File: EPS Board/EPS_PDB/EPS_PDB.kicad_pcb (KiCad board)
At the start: 2 copper layers, 92 x 92 mm, 125 parts, among them J1 USB_B_Micro, J2 Conn_02x26_Odd_Even, J3 Conn_02x26_Odd_Even, J4 Conn_01x04_Pin, Q1 PMOS, Q2 PMOS, SW1 SW_SPDT, U1 AMS1117-3.3, U10 TPS259621DDAT, U11 LM5000-3MTCX, U12 TPS259621DDAT, U13 TPS259621DDAT, U14 AD7708BRUZ, U15 TPS259621DDAT, U16 TPS259621DDAT, U17 LTC3624EMSE-3.3PBF, U18 TPS259621DDAT, U19 LTC3624IDD-25PBF, U2 SN65HVD256D, U3 SN65HVD256D, U4 STM32L476VET6, U5 TPS3824-33QDBVRQ1, U6 TS4061BICT-1.25, U7 TPS259621DDAT, U8 TPS259621DDAT, U9 TPS259621DDAT, Y1 32MHz, Y2 32.768kHz

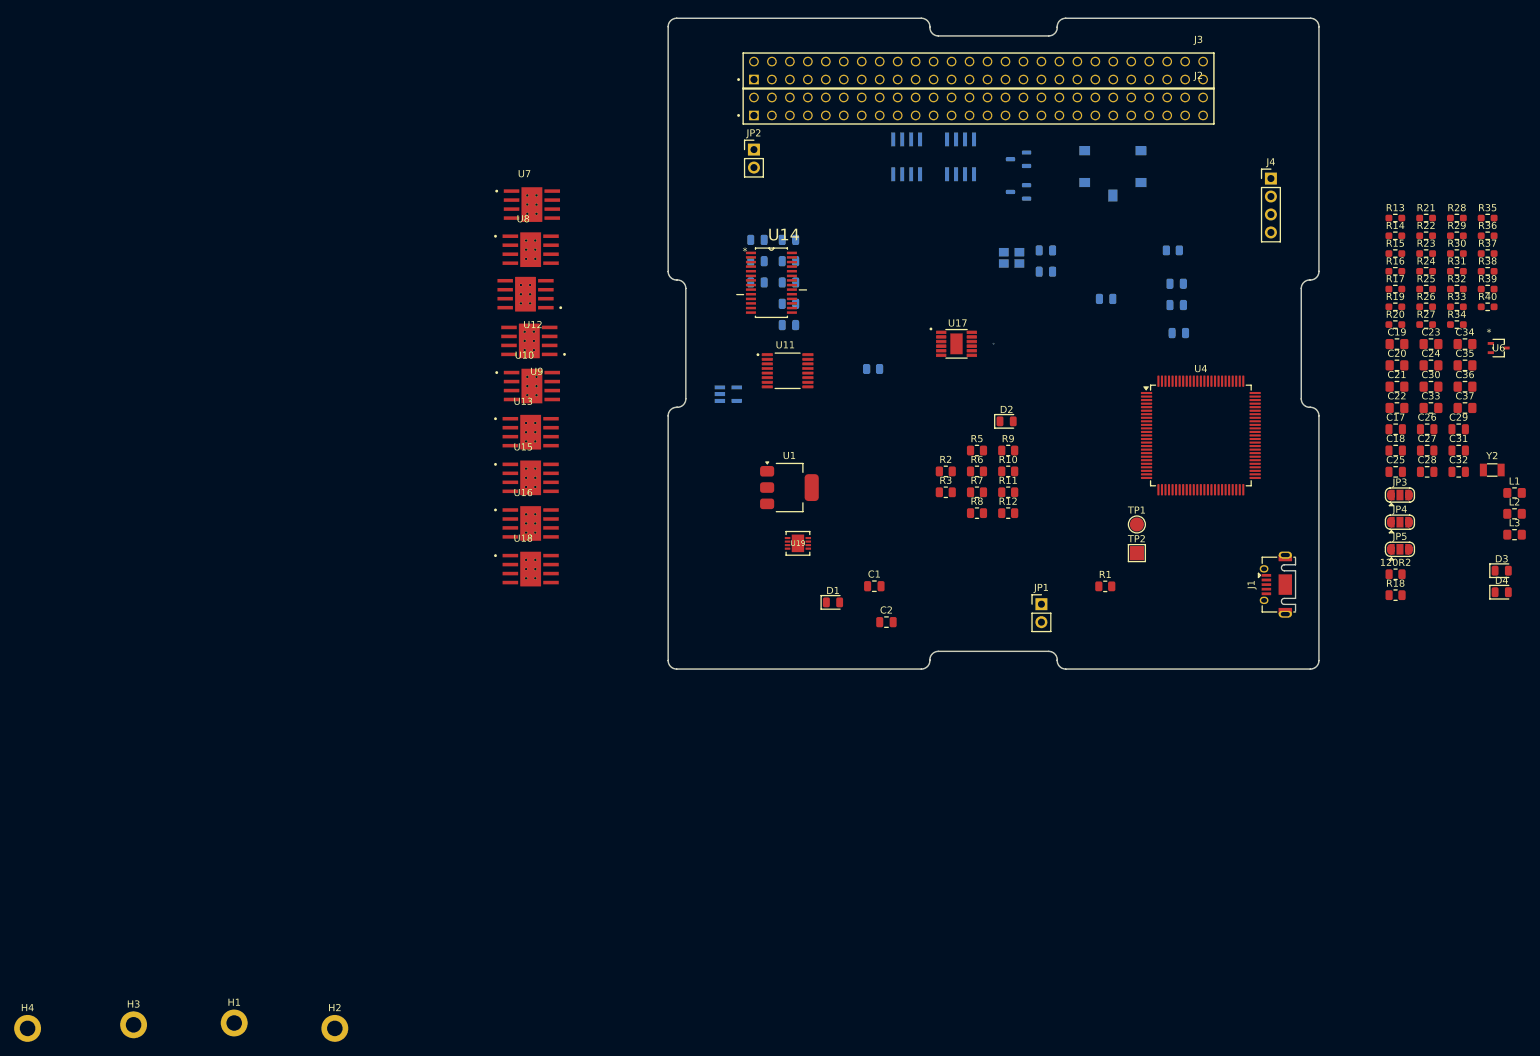
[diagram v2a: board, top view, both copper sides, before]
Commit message: PDB PCB Design Progress
Board outline copy pasted from Antenna Deployment Board
Added current limiter datasheet
Routed USB differential pair
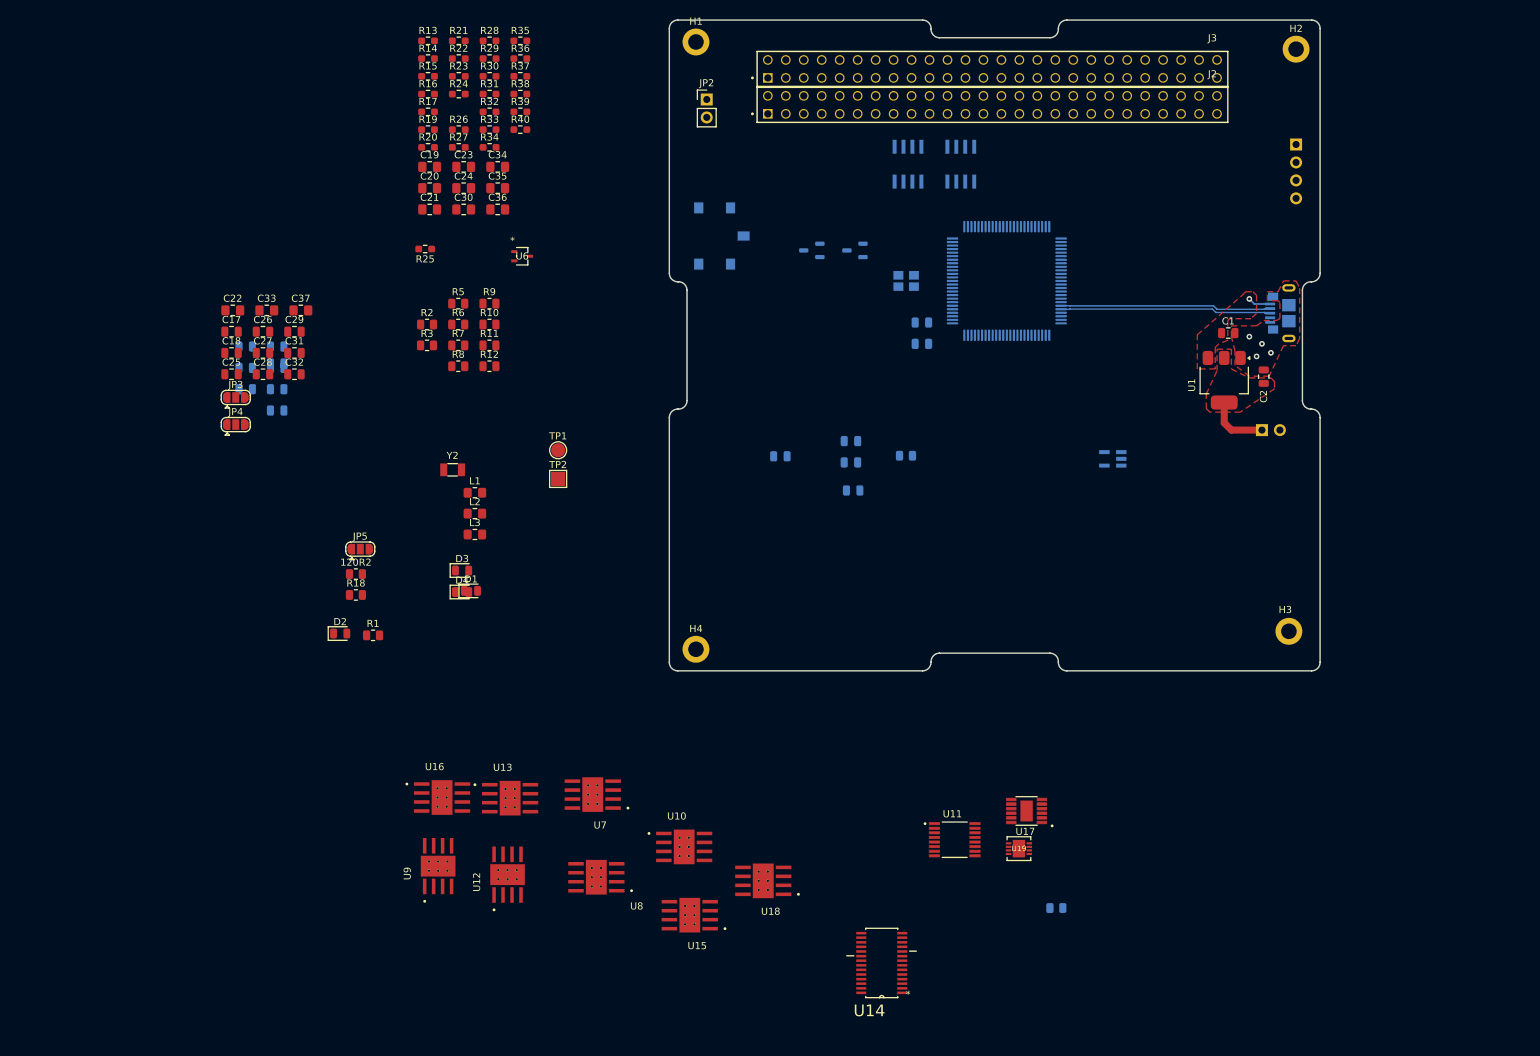
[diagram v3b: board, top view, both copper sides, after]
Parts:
- J1: footprint Connector_USB:USB_Micro-AB_Molex_47590-0001 -> Connector_USB:USB_Micro-B_GCT_USB3076-30-A; moved to B.Cu
- J4, JP1, U4: moved to B.Cu
- U10: value TPS259621DDAT -> TPS259621DDAT_5V_PAY
- U12: value TPS259621DDAT -> TPS259621DDAT_5V_EPS
- U13: value TPS259621DDAT -> TPS259621DDAT_5V_OBC
- U15: value TPS259621DDAT -> TPS259621DDAT_5V_ADCS
- U16: value TPS259621DDAT -> TPS259621DDAT_5V_COMM
- U18: value TPS259621DDAT -> TPS259621DDAT_12V_ADCS
- U7: value TPS259621DDAT -> TPS259621DDAT 3V3_ADCS
- U8: value TPS259621DDAT -> TPS259621DDAT_3V3_ANT
- U9: value TPS259621DDAT -> TPS259621DDAT_3V3_EPS
- moved H2 194.0 mm to (202.2, 49.8)
- moved H3 172.5 mm to (201.2, 132.1)
- moved C22 165.2 mm to (51.9, 86.7)
- moved C29 165.2 mm to (60.6, 89.7)
- moved C31 165.2 mm to (60.6, 92.7)
- moved C32 165.2 mm to (60.6, 95.7)
- moved C33 165.2 mm to (56.7, 86.7)
- moved C17 165.2 mm to (51.7, 89.7)
- moved C18 165.2 mm to (51.7, 92.7)
- moved C25 165.2 mm to (51.7, 95.7)
- moved C26 165.2 mm to (56.1, 89.7)
- moved C27 165.2 mm to (56.1, 92.7)
- moved C28 165.2 mm to (56.1, 95.7)
- moved C37 165.2 mm to (61.5, 86.7)
- moved JP3 165.2 mm to (52.3, 99.0)
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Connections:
- net Net-(U11-FB) renamed /EPS Power Distribution/12V
- net Net-(U11-VIN) renamed /EPS Power Distribution/VIN
- J1 pad 6: unconnected-(J1-Shield-Pad6) -> GND
- U4 pad 70: /EPS Control Unit/USB_D- -> /USB_D-
- U4 pad 71: /EPS Control Unit/USB_D+ -> /USB_D+
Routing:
- net /USB_D-: track 0.00 -> 30.1 mm
- net /USB_D+: track 0.00 -> 30.1 mm
- net /3V3_LDO: track 0.00 -> 8.63 mm
- net VBUS: track 0.00 -> 3.57 mm, vias 0 -> 1
- net GND: vias 0 -> 4
- added copper zone on F.Cu, net /3V3_LDO
- added copper zone on F.Cu, net GND
- added copper zone on In1.Cu, net GND
- added copper zone on F.Cu, net VBUS
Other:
- outline, holes or cut-outs redrawn
- copper layers 2 -> 4
- board text added: "4 LAYER BOARD SIG+PWR GND GND SIG"

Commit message: EPS PDB Board Layout Progress
Fixed issue with outline,
added correct outline
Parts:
- added D5: EPS_5V_LED, LED_SMD:LED_0805_2012Metric, B.Cu at (167.7, 102.4)
- added JP6: USB_POW_EN, Connector_PinHeader_2.54mm:PinHeader_1x02_P2.54mm_Vertical, F.Cu at (187.8, 82.4)
- added R41: 1k5, Resistor_SMD:R_0603_1608Metric, B.Cu at (163.5, 102.4)
- C1, C2: footprint Capacitor_SMD:C_0805_2012Metric -> Capacitor_SMD:C_0603_1608Metric; moved to B.Cu
- C10, C11, C12, C13, C14, C15, C16, C17, C18, C25, C26, C27, C28, C29, C3, C31, C32, C4, C5, C6, C7, C8, C9: footprint Capacitor_SMD:C_0805_2012Metric -> Capacitor_SMD:C_0603_1608Metric
- C19, C20, C21, C22, C23, C24, C30, C33, C34, C35, C36, C37: footprint Capacitor_SMD:C_0805_2012Metric_Pad1.18x1.45mm_HandSolder -> Capacitor_SMD:C_0603_1608Metric
- D1: value POWER_LED -> EPS_3V3_LED; moved to B.Cu
- D2, U1: moved to B.Cu
- H1, H2, H3, H4: footprint MountingHole:MountingHole_2.2mm_M2_DIN965_Pad -> MountingHole:MountingHole_3.2mm_M3_Pad
- J4: footprint Connector_PinHeader_2.54mm:PinHeader_1x04_P2.54mm_Vertical -> Connector_PinHeader_2.54mm:PinHeader_1x04_P2.54mm_Horizontal; moved to F.Cu
- JP1: moved to F.Cu
- R1, R11, R12, R7, R8: footprint Resistor_SMD:R_0805_2012Metric -> Resistor_SMD:R_0603_1608Metric; moved to B.Cu
- R10, R18, R2, R3, R4, R5, R6, R9: footprint Resistor_SMD:R_0805_2012Metric -> Resistor_SMD:R_0603_1608Metric
- R13, R14, R15, R16, R17, R19, R20, R21, R22, R23, R24, R25, R26, R27, R28, R29, R30, R31, R32, R33, R34, R35, R36, R37, R38, R39, R40: footprint Resistor_SMD:R_0603_1608Metric_Pad0.98x0.95mm_HandSolder -> Resistor_SMD:R_0603_1608Metric
- moved U10 219.2 mm to (-102.7, 143.9)
- moved U11 219.2 mm to (-64.4, 142.9)
- moved U12 219.2 mm to (-127.7, 147.8)
- moved U13 219.2 mm to (-127.3, 137.0)
- moved U14 219.2 mm to (-74.7, 160.3)
- moved U15 219.2 mm to (-101.9, 153.6)
- moved U16 219.2 mm to (-136.9, 136.9)
- moved U17 219.2 mm to (-54.3, 138.8)
- moved U18 219.2 mm to (-91.5, 148.7)
- moved U19 219.2 mm to (-55.4, 144.1)
- moved U7 219.2 mm to (-115.6, 136.5)
- moved U8 219.2 mm to (-115.1, 148.2)
- moved U9 219.2 mm to (-137.5, 146.6)
- moved TP1 176.3 mm to (-78.3, 112.2)
- moved TP2 176.3 mm to (-78.3, 116.2)
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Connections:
- C1 pad 1: VBUS -> VUSB
- C34 pad 1: VBUS -> /VBUS
- C36 pad 1: VBUS -> /VBUS
- J1 pad 1: VBUS -> VUSB
- J1 pad 6: GND -> unconnected-(J1-Shield-Pad6)_5
- J3 pad 52: /I2C2_SDA -> /I2C1_SDA
- JP2 pad 2: VBUS -> /VBUS
- JP3 pad 2: Net-(JP3-C) -> Net-(JP3-B)
- JP5 pad 2: Net-(JP5-C) -> Net-(JP5-B)
- L1 pad 1: VBUS -> /VBUS
- R25 pad 2: VBUS -> /VBUS
- R8 pad 2: /I2C2_SDA -> /I2C1_SDA
- U1 pad 3: VBUS -> VUSB
- U17 pad 10: Net-(JP3-C) -> Net-(JP3-B)
- U19 pad 7: Net-(JP5-C) -> Net-(JP5-B)
- U4 pad 72: /EPS Control Unit/SWDIO -> /SWDIO
- U4 pad 76: /EPS Control Unit/SWCLK -> /SWCLK
- U4 pad 96: /I2C2_SDA -> /I2C1_SDA
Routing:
- net /UART1_TX: track 0.00 -> 70.4 mm
- net /I2C1_SDA: track 0.00 -> 62.3 mm, vias 0 -> 2
- net /UART1_RX: track 0.00 -> 60.5 mm
- net /I2C1_SCL: track 0.00 -> 59.7 mm, vias 0 -> 2
- net /UART1_RTS: track 0.00 -> 40.8 mm, vias 0 -> 1
- net /UART1_CTS: track 0.00 -> 38.6 mm, vias 0 -> 1
- net /I2C2_SDA: track 0.00 -> 33.0 mm
- net /I2C2_SCL: track 0.00 -> 32.0 mm
- net GND: track 0.00 -> 21.1 mm, vias 4 -> 9
- net /EPS Control Unit/NRST: track 0.00 -> 16.6 mm
- net 3V3_EPS: track 0.00 -> 13.5 mm
- net /EPS Control Unit/HSE_IN: track 0.00 -> 12.6 mm
- net /USB_D+: track 30.1 -> 41.4 mm
- net /USB_D-: track 30.1 -> 41.4 mm
- net /EPS Control Unit/HSE_OUT: track 0.00 -> 9.41 mm
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- added copper zone on In2.Cu, net GND
- removed copper zone on F.Cu, net /3V3_LDO
- removed copper zone on F.Cu, net GND
- removed copper zone on F.Cu, net VBUS

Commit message: EPS PDB Layout
Power Distribution and Regulation unit layout started
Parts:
- L1, L2: footprint Inductor_SMD:L_0805_2012Metric_Pad1.15x1.40mm_HandSolder -> Inductor_SMD:L_Wuerth_WE-XHMI-8080
- L3: footprint Inductor_SMD:L_0805_2012Metric_Pad1.15x1.40mm_HandSolder -> Inductor_SMD:L_1206_3216Metric
- R2, R3, R5, R6: moved to B.Cu
- SW1: footprint Button_Switch_SMD:SW_SPST_B3S-1100 -> Button_Switch_SMD:SW_SPST_B3U-1100P
- moved R5 337.2 mm to (244.4, 105.5), turned to 180 degrees
- moved R3 325.6 mm to (228.7, 101.3)
- moved R2 322.6 mm to (225.4, 107.4), turned to 180 degrees
- moved U16 322.4 mm to (183.6, 102.3), turned to 90 degrees
- moved U13 303.5 mm to (174.3, 102.5), turned to 90 degrees
- moved JP4 303.4 mm to (176.4, 65.1)
- moved U15 302.3 mm to (194.8, 95.3), turned to 90 degrees
- moved C18 297.7 mm to (171.7, 69.5), turned to 45 degrees
- moved U12 295.7 mm to (164.6, 102.6)
- moved C17 295.1 mm to (169.6, 71.7), turned to -135 degrees
- moved U18 286.9 mm to (193.5, 115.2), turned to 90 degrees
- moved U9 273.8 mm to (132.8, 102.7)
- moved JP3 273.5 mm to (149.1, 121.3)
- moved R6 271.8 mm to (178.5, 73.6), turned to 180 degrees
- moved U14 267.4 mm to (177.8, 72.3), turned to 135 degrees
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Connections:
- net Net-(Q1-G) renamed /EPS Control Unit/PMOS1_GATE
- net Net-(Q2-G) renamed /EPS Control Unit/PMOS2_GATE
- JP3 pad 2: Net-(JP3-B) -> /EPS Power Distribution/MODE
- U17 pad 10: Net-(JP3-B) -> /EPS Power Distribution/MODE
- U19 pad 5: /EPS Power Distribution/5V_BUS -> unconnected-(U19-FB-Pad5)
- U19 pad 6: Net-(JP5-B) -> unconnected-(U19-INTVCC-Pad6)
- U19 pad 7: Net-(JP5-B) -> unconnected-(U19-MODE/SYNC-Pad7)
- U19 pad 8: GND -> unconnected-(U19-GND_2-Pad8)
- U19 pad 9: GND -> unconnected-(U19-GND-Pad9)
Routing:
- net 3V3_EPS: track 13.5 -> 127.4 mm, vias 0 -> 4
- net /12V_ADCS: track 0.00 -> 80.3 mm, vias 0 -> 2
- net /3V3_ADCS: track 0.00 -> 77.6 mm, vias 0 -> 2
- net /HEARTBEAT_OBC: track 0.00 -> 63.8 mm
- net /HEARTBEAT_ADCS: track 0.00 -> 63.8 mm
- net /5V_ADCS: track 0.00 -> 58.2 mm, vias 0 -> 2
- net /5V_OBC: track 0.00 -> 53.8 mm, vias 0 -> 2
- net /5V_PAY: track 0.00 -> 53.7 mm, vias 0 -> 2
- net /3V3_ANT: track 0.00 -> 53.4 mm
- net /ANT_DEPLOY_STATUS: track 0.00 -> 50.3 mm, vias 0 -> 2
- net /EPS Control Unit/SW_BOOT0: track 0.00 -> 48.4 mm, vias 0 -> 2
- net /ANT_DEPLOY: track 0.00 -> 47.6 mm, vias 0 -> 2
- net /SWCLK: track 0.00 -> 46.5 mm, vias 0 -> 1
- net 5V_EPS: track 0.00 -> 45.5 mm, vias 0 -> 2
- net /SWDIO: track 0.00 -> 45.2 mm, vias 0 -> 1
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- added copper zone on F.Cu, net /3V3_ADCS
- added copper zone on F.Cu, net /3V3_ANT
- added copper zone on B.Cu, net /3V3_LDO
- added copper zone on F.Cu, net /5V_ADCS
- added copper zone on F.Cu, net /5V_COMM
- added copper zone on F.Cu, net /VBUS0
- added copper zone on B.Cu, net GND
- added copper zone on B.Cu, net VUSB

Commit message: Progresss in EPS PDB Layout
Voltage Converters and Current limiter section pending
Might need to increase trace width of power traces on inner layers
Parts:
- removed TP1: TestPoint, TestPoint:TestPoint_Pad_D2.0mm
- removed TP2: TestPoint, TestPoint:TestPoint_Pad_2.0x2.0mm
- moved C27 136.9 mm to (176.2, 80.8), turned to -135 degrees
- moved C28 136.5 mm to (175.2, 79.8), turned to -135 degrees
- moved C26 133.3 mm to (171.1, 69.3), turned to 45 degrees
- moved C29 132.6 mm to (177.0, 83.6), turned to 135 degrees
- moved C25 122.5 mm to (172.2, 70.4), turned to 45 degrees
- moved R40 122.2 mm to (192.1, 108.9)
- moved R36 119.7 mm to (190.6, 95.5), turned to -90 degrees
- moved R38 117.1 mm to (190.8, 90.5), turned to 45 degrees
- moved 120R2 111.0 mm to (178.3, 82.4), turned to -45 degrees
- moved R37 110.9 mm to (179.5, 102.7), turned to -90 degrees
- moved R39 109.7 mm to (182.1, 96.7)
- moved R35 104.3 mm to (172.8, 96.6)
- moved R33 103.4 mm to (170.1, 102.5), turned to -90 degrees
- moved L1 102.2 mm to (173.3, 117.7), turned to 90 degrees
- moved R3 96.8 mm to (136.2, 72.6), turned to 90 degrees
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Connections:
- R33 pad 2: unconnected-(R33-Pad2) -> GND
- U19 pad 5: unconnected-(U19-FB-Pad5) -> /EPS Power Distribution/5V_BUS
- U19 pad 6: unconnected-(U19-INTVCC-Pad6) -> Net-(JP5-B)
- U19 pad 7: unconnected-(U19-MODE/SYNC-Pad7) -> Net-(JP5-B)
- U19 pad 8: unconnected-(U19-GND_2-Pad8) -> GND
- U19 pad 9: unconnected-(U19-GND-Pad9) -> GND
- U4 pad 77: unconnected-(U4-PA15-Pad77) -> /RESET_ADC
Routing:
- net /EPS Power Distribution/ILM_3V3_ANT: track 0.00 -> 73.6 mm, vias 0 -> 2
- net /EPS Power Distribution/ILM_3V3_EPS: track 0.00 -> 72.2 mm, vias 0 -> 2
- net /EPS Power Distribution/ILM_5V_PAY: track 0.00 -> 57.7 mm, vias 0 -> 2
- net /RESET_ADC: track 0.00 -> 55.9 mm, vias 0 -> 4
- net /EPS Power Distribution/ILM_3V3_ADCS: track 0.00 -> 54.9 mm, vias 0 -> 2
- net /EPS Control Unit/CAN_SW_A: track 0.00 -> 49.9 mm, vias 0 -> 6
- net /EPS Power Distribution/ILM_12V_ADCS: track 0.00 -> 48.8 mm, vias 0 -> 2
- net /EPS Control Unit/CAN_SW_B: track 0.00 -> 46.8 mm, vias 0 -> 4
- net /EPS Power Distribution/ILM_5V_EPS: track 0.00 -> 44.4 mm, vias 0 -> 2
- net /EPS Power Distribution/ILM_5V_OBC: track 0.00 -> 37.6 mm, vias 0 -> 2
- net /FLT_5V_ADCS: track 0.00 -> 33.9 mm, vias 0 -> 1
- net /FLT_5V_PAY: track 0.00 -> 32.1 mm, vias 0 -> 2
- net /EPS Control Unit/EPS_LED: track 0.00 -> 30.7 mm, vias 0 -> 4
- net 5V_EPS: track 45.5 -> 75.6 mm, vias 2 -> 7
- net /EPS Power Distribution/ILM_5V_ADCS: track 0.00 -> 26.3 mm, vias 0 -> 2
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- added copper zone on F.Cu, net GND
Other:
- board text added: "EPS POWER DISTRIBUTION BOARD"
